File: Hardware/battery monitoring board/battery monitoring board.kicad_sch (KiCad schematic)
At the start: 10 parts, among them J1 Conn_01x02, J2 Conn_01x02, U1 MCP3008

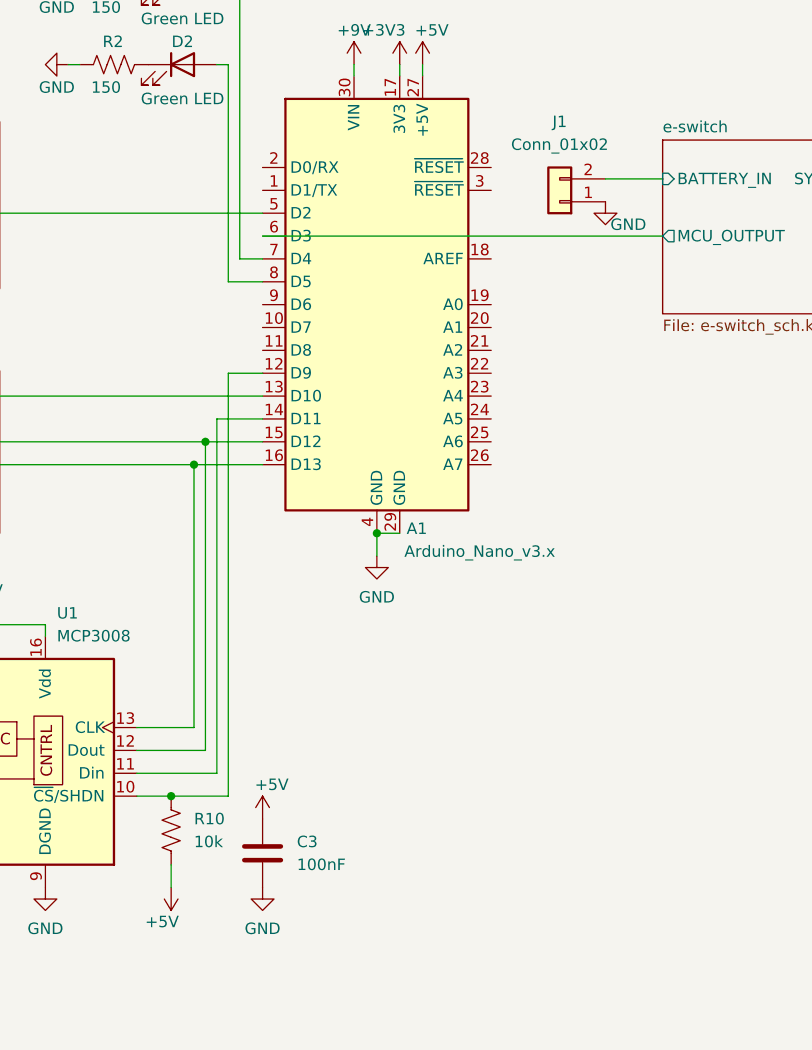
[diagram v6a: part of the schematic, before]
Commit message: resolved erc/drc issues
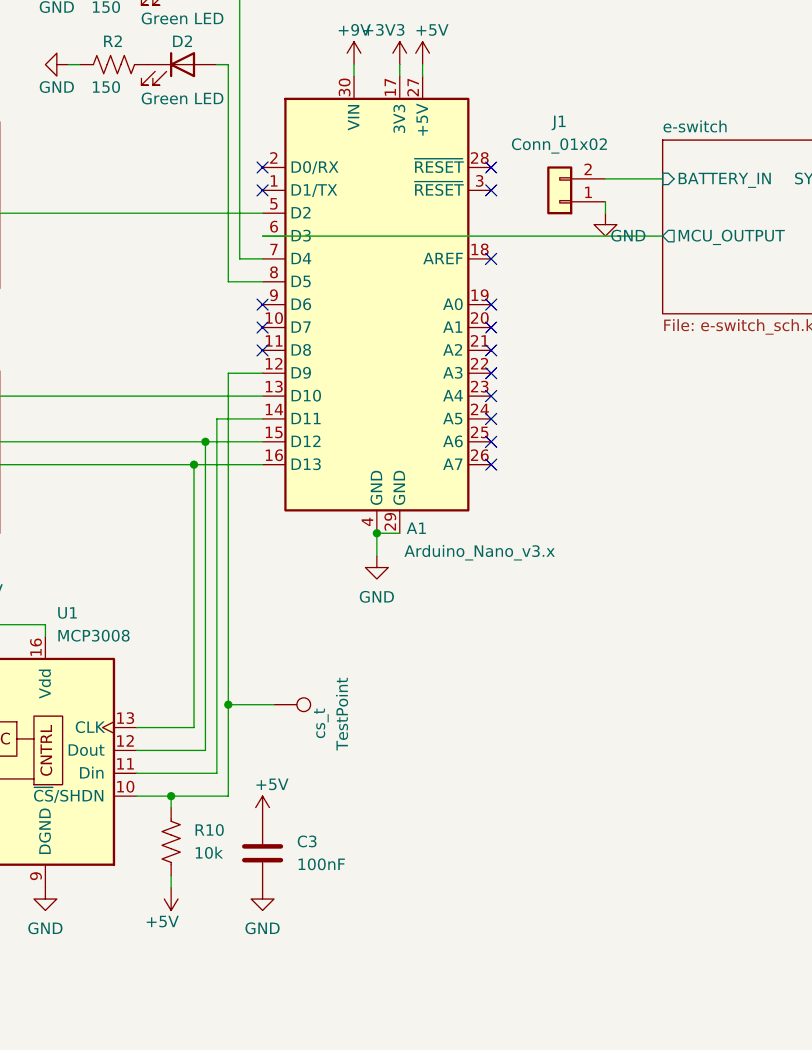
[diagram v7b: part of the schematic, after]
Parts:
- added cs_t: TestPoint, PCM_4ms_TestPoint:TestPoint_Pad_06, symbol Connector:TestPoint
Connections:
- net at A1.12 (D9), R10.1, U1.10 (~{CS}/SHDN): now also cs_t.1
- no-connect marks 0 -> 16
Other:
- moved on the sheet: R10
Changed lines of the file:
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@@
   (junction (at 101.6 102.87) (diameter 0) (color 0 0 0 0)
   )
+  (junction (at 105.41 129.54) (diameter 0) (color 0 0 0 0)
+  )
+  (no_connect (at 134.62 72.39))
+  (no_connect (at 134.62 102.87))
+  (no_connect (at 134.62 80.01))
+  (no_connect (at 134.62 69.85))
+  (no_connect (at 109.22 85.09))
+  (no_connect (at 134.62 90.17))
+  (no_connect (at 109.22 87.63))
+  (no_connect (at 109.22 90.17))
+  (no_connect (at 134.62 87.63))
+  (no_connect (at 134.62 97.79))
+  (no_connect (at 134.62 85.09))
+  (no_connect (at 134.62 92.71))
+  (no_connect (at 134.62 95.25))
+  (no_connect (at 109.22 72.39))
+  (no_connect (at 109.22 69.85))
+  (no_connect (at 134.62 100.33))
   (wire (pts (xy 77.47 120.65) (xy 77.47 121.92))
     (stroke (width 0) (type default))
@@
     (stroke (width 0) (type default))
   )
+  (wire (pts (xy 147.32 74.93) (xy 147.32 73.66))
+    (stroke (width 0) (type default))
+  )
   (wire (pts (xy 77.47 120.65) (xy 85.09 120.65))
     (stroke (width 0) (type default))
@@
     (stroke (width 0) (type default))
   )
+  (wire (pts (xy 105.41 129.54) (xy 110.49 129.54))
+    (stroke (width 0) (type default))
+  )
+  (wire (pts (xy 105.41 129.54) (xy 105.41 92.71))
+    (stroke (width 0) (type default))
+  )
   (wire (pts (xy 106.68 80.01) (xy 109.22 80.01))
     (stroke (width 0) (type default))
@@
     (stroke (width 0) (type default))
   )
-  (wire (pts (xy 99.06 149.86) (xy 99.06 147.32))
+  (wire (pts (xy 99.06 149.86) (xy 99.06 148.59))
     (stroke (width 0) (type default))
   )
@@
     (stroke (width 0) (type default))
   )
-  (wire (pts (xy 105.41 139.7) (xy 105.41 92.71))
+  (wire (pts (xy 105.41 139.7) (xy 105.41 129.54))
     (stroke (width 0) (type default))
   )
@@
   )
   (wire (pts (xy 80.01 74.93) (xy 109.22 74.93))
+    (stroke (width 0) (type default))
+  )
+  (wire (pts (xy 99.06 140.97) (xy 99.06 139.7))
     (stroke (width 0) (type default))
   )
@@
     )
   )
-  (symbol (lib_id "Device:R_US") (at 99.06 143.51 0) (unit 1)
+  (symbol (lib_id "Device:R_US") (at 99.06 144.78 0) (unit 1)
     (in_bom yes) (on_board yes) (dnp no) (fields_autoplaced)
-    (property "Reference" "R10" (at 101.6 142.24 0)
-      (effects (font (size 1.27 1.27)) (justify left))
-    )
-    (property "Value" "10k" (at 101.6 144.78 0)
-      (effects (font (size 1.27 1.27)) (justify left))
-    )
-    (property "Footprint" "Resistor_SMD:R_0805_2012Metric_Pad1.20x1.40mm_HandSolder" (at 100.076 143.764 90)
-      (effects (font (size 1.27 1.27)) hide)
-    )
-    (property "Datasheet" "~" (at 99.06 143.51 0)
+    (property "Reference" "R10" (at 101.6 143.51 0)
+      (effects (font (size 1.27 1.27)) (justify left))
+    )
+    (property "Value" "10k" (at 101.6 146.05 0)
+      (effects (font (size 1.27 1.27)) (justify left))
+    )
+    (property "Footprint" "Resistor_SMD:R_0805_2012Metric_Pad1.20x1.40mm_HandSolder" (at 100.076 145.034 90)
+      (effects (font (size 1.27 1.27)) hide)
+    )
+    (property "Datasheet" "~" (at 99.06 144.78 0)
       (effects (font (size 1.27 1.27)) hide)
     )
@@
     )
   )
-  (symbol (lib_id "PCM_4ms_Power-symbol:GND") (at 147.32 73.66 0) (unit 1)
-    (in_bom yes) (on_board yes) (dnp no)
-    (property "Reference" "#PWR012" (at 147.32 80.01 0)
-      (effects (font (size 1.27 1.27)) hide)
-    )
-    (property "Value" "GND" (at 149.86 76.2 0)
-      (effects (font (size 1.27 1.27)))
-    )
-    (property "Footprint" "" (at 147.32 73.66 0)
-      (effects (font (size 1.27 1.27)) hide)
-    )
-    (property "Datasheet" "" (at 147.32 73.66 0)
+  (symbol (lib_id "PCM_4ms_Power-symbol:GND") (at 147.32 74.93 0) (unit 1)
+    (in_bom yes) (on_board yes) (dnp no)
+    (property "Reference" "#PWR012" (at 147.32 81.28 0)
+      (effects (font (size 1.27 1.27)) hide)
+    )
+    (property "Value" "GND" (at 149.86 77.47 0)
+      (effects (font (size 1.27 1.27)))
+    )
+    (property "Footprint" "" (at 147.32 74.93 0)
+      (effects (font (size 1.27 1.27)) hide)
+    )
+    (property "Datasheet" "" (at 147.32 74.93 0)
       (effects (font (size 1.27 1.27)) hide)
     )
@@
         )
       )
+    )
+  )
+  (symbol (lib_id "Connector:TestPoint") (at 110.49 129.54 270) (unit 1)
+    (in_bom yes) (on_board yes) (dnp no)
+    (property "Reference" "cs_t" (at 115.57 133.35 0)
+      (effects (font (size 1.27 1.27)) (justify right))
+    )
+    (property "Value" "TestPoint" (at 118.11 134.62 0)
+      (effects (font (size 1.27 1.27)) (justify right))
+    )
+    (property "Footprint" "PCM_4ms_TestPoint:TestPoint_Pad_06" (at 110.49 134.62 0)
+      (effects (font (size 1.27 1.27)) hide)
+    )
+    (property "Datasheet" "~" (at 110.49 134.62 0)
+      (effects (font (size 1.27 1.27)) hide)
+    )
+    (pin "1")
+    (instances
+      (project "battery monitoring board"
+        (path "/bf623d80-ca5a-491f-9daa-4dffbeba5279/5ec2dbdf-a276-4d4c-99fc-008475c1e770"
+          (reference "cs_t") (unit 1)
+        )
+        (path "/bf623d80-ca5a-491f-9daa-4dffbeba5279"
+          (reference "cs_adc1") (unit 1)
+        )
+      )
